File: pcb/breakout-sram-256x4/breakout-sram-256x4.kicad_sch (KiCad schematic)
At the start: 24 parts, among them U1 IS61WV25616-10TLI, U2 IS61WV25616-10TLI, U3 IS61WV25616-10TLI, U4 IS61WV25616-10TLI

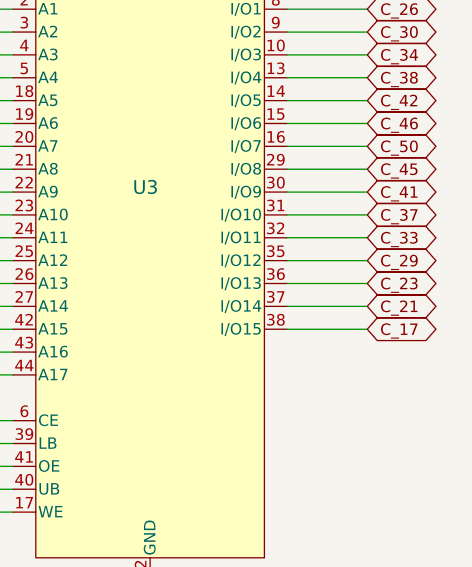
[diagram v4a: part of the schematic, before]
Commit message: [sram_4x][pcb] fix C_25 net label
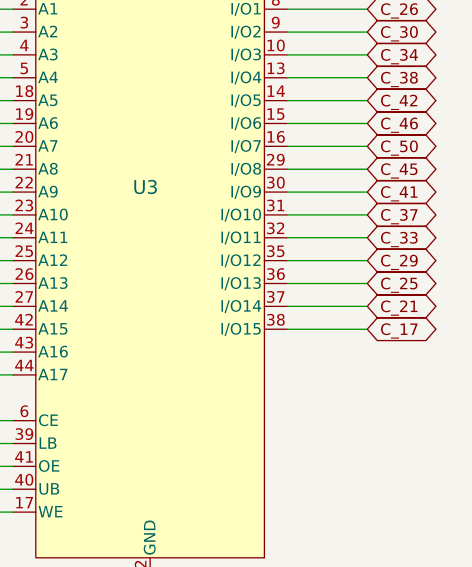
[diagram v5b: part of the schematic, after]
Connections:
- net C_23 renamed C_25
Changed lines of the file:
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@@
 		)
 	)
-	(global_label "C_23"
+	(global_label "C_25"
 		(shape bidirectional)
 		(at 264.16 95.25 0)
@@
 		)
 		(property "Intersheetrefs" "${INTERSHEET_REFS}"
-			(at 272.7317 95.25 0)
+			(at 272.9131 95.25 0)
 			(effects
 				(font

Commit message: [sram_4x][pcb] pull in traces and edge cut for more clearance
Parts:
- U1, U2, U3, U4: footprint IS61WV25616-10TLI:44L_TSOP-2_400_ISI -> 44L_TSOP-2_400_ISI
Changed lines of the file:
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@@
 			)
 		)
-		(property "Footprint" "IS61WV25616-10TLI:44L_TSOP-2_400_ISI"
+		(property "Footprint" "44L_TSOP-2_400_ISI"
 			(at 128.27 62.23 0)
 			(effects
@@
 			)
 		)
-		(property "Footprint" "IS61WV25616-10TLI:44L_TSOP-2_400_ISI"
+		(property "Footprint" "44L_TSOP-2_400_ISI"
 			(at 220.98 176.53 0)
 			(effects
@@
 			)
 		)
-		(property "Footprint" "IS61WV25616-10TLI:44L_TSOP-2_400_ISI"
+		(property "Footprint" "44L_TSOP-2_400_ISI"
 			(at 129.54 176.53 0)
 			(effects
@@
 			)
 		)
-		(property "Footprint" "IS61WV25616-10TLI:44L_TSOP-2_400_ISI"
+		(property "Footprint" "44L_TSOP-2_400_ISI"
 			(at 219.71 62.23 0)
 			(effects
